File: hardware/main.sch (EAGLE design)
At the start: 10 parts, among them U1 TXB0101_DBV_6

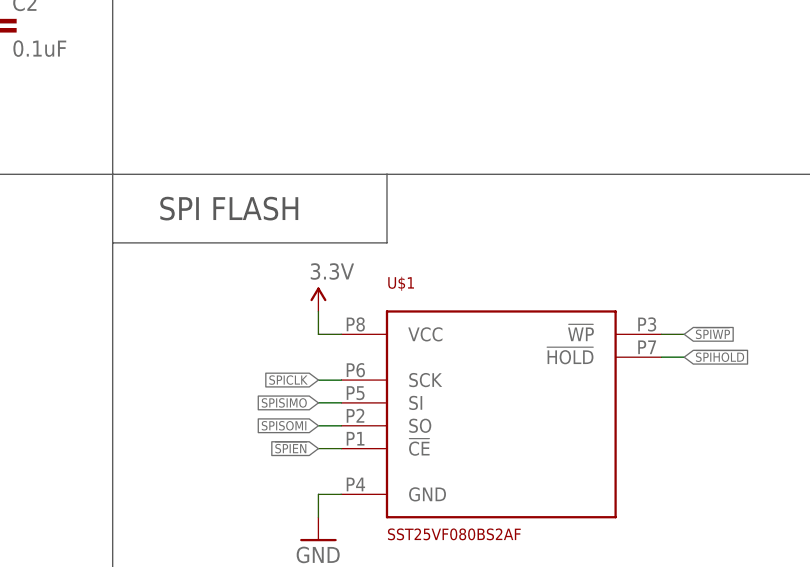
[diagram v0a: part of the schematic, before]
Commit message: Updated small labels. Cleaned up silkscreen layer.
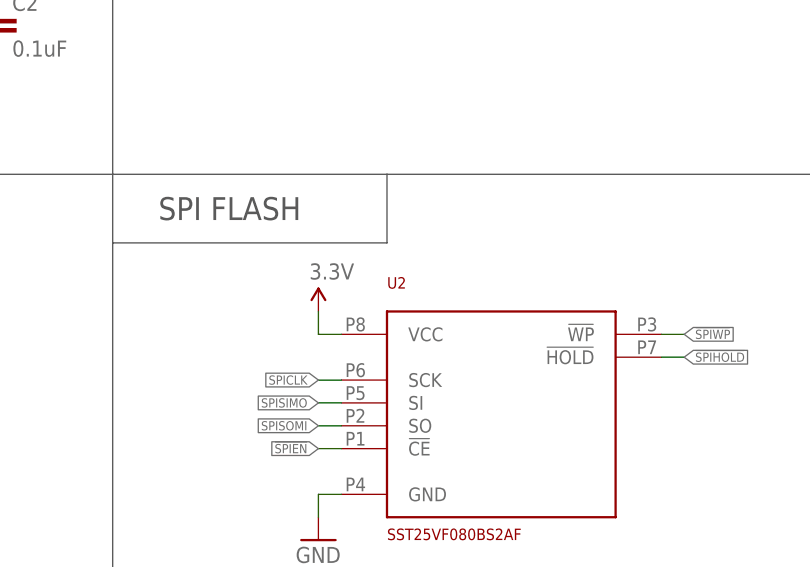
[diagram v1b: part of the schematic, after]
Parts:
- renumbered U$1 to U2
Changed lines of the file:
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@@
 <part name="R2" library="SparkFun-Resistors" deviceset="RESISTOR" device="0805-RES" value="10k"/>
 <part name="C2" library="SparkFun-Capacitors" deviceset="1.0UF-25V-+80/-20(0805)" device="" value="0.1uF"/>
-<part name="U$1" library="ControllerCard" deviceset="SST25VF080B" device="S2AF"/>
+<part name="U2" library="ControllerCard" deviceset="SST25VF080B" device="S2AF"/>
 <part name="SUPPLY6" library="SparkFun-Aesthetics" deviceset="3.3V" device=""/>
 <part name="GND6" library="SparkFun-Aesthetics" deviceset="GND" device=""/>
@@
 <instance part="R2" gate="G$1" x="104.14" y="71.12" rot="R90"/>
 <instance part="C2" gate="G$1" x="119.38" y="68.58"/>
-<instance part="U$1" gate="G$1" x="175.26" y="25.4"/>
+<instance part="U2" gate="G$1" x="175.26" y="25.4"/>
 <instance part="SUPPLY6" gate="G$1" x="154.94" y="38.1"/>
 <instance part="GND6" gate="1" x="154.94" y="12.7"/>
@@
 </segment>
 <segment>
-<pinref part="U$1" gate="G$1" pin="VCC"/>
+<pinref part="U2" gate="G$1" pin="VCC"/>
 <pinref part="SUPPLY6" gate="G$1" pin="3.3V"/>
 <wire x1="157.48" y1="35.56" x2="154.94" y2="35.56" width="0.1524" layer="91"/>
@@
 </segment>
 <segment>
-<pinref part="U$1" gate="G$1" pin="GND"/>
+<pinref part="U2" gate="G$1" pin="GND"/>
 <pinref part="GND6" gate="1" pin="GND"/>
 <wire x1="157.48" y1="17.78" x2="154.94" y2="17.78" width="0.1524" layer="91"/>
@@
 <net name="SPICLK" class="0">
 <segment>
-<pinref part="U$1" gate="G$1" pin="SCK"/>
+<pinref part="U2" gate="G$1" pin="SCK"/>
 <wire x1="157.48" y1="30.48" x2="154.94" y2="30.48" width="0.1524" layer="91"/>
 <label x="154.94" y="30.48" size="1.016" layer="95" rot="R180" xref="yes"/>
@@
 <net name="SPISIMO" class="0">
 <segment>
-<pinref part="U$1" gate="G$1" pin="SI"/>
+<pinref part="U2" gate="G$1" pin="SI"/>
 <wire x1="157.48" y1="27.94" x2="154.94" y2="27.94" width="0.1524" layer="91"/>
 <label x="154.94" y="27.94" size="1.016" layer="95" rot="R180" xref="yes"/>
@@
 <net name="SPISOMI" class="0">
 <segment>
-<pinref part="U$1" gate="G$1" pin="SO"/>
+<pinref part="U2" gate="G$1" pin="SO"/>
 <wire x1="157.48" y1="25.4" x2="154.94" y2="25.4" width="0.1524" layer="91"/>
 <label x="154.94" y="25.4" size="1.016" layer="95" rot="R180" xref="yes"/>
@@
 <net name="!SPIEN!" class="0">
 <segment>
-<pinref part="U$1" gate="G$1" pin="!CE!"/>
+<pinref part="U2" gate="G$1" pin="!CE!"/>
 <wire x1="157.48" y1="22.86" x2="154.94" y2="22.86" width="0.1524" layer="91"/>
 <label x="154.94" y="22.86" size="1.016" layer="95" rot="R180" xref="yes"/>
@@
 <net name="!SPIWP!" class="0">
 <segment>
-<pinref part="U$1" gate="G$1" pin="!WP!"/>
+<pinref part="U2" gate="G$1" pin="!WP!"/>
 <wire x1="193.04" y1="35.56" x2="195.58" y2="35.56" width="0.1524" layer="91"/>
 <label x="195.58" y="35.56" size="1.016" layer="95" xref="yes"/>
@@
 <net name="!SPIHOLD!" class="0">
 <segment>
-<pinref part="U$1" gate="G$1" pin="!HOLD!"/>
+<pinref part="U2" gate="G$1" pin="!HOLD!"/>
 <wire x1="193.04" y1="33.02" x2="195.58" y2="33.02" width="0.1524" layer="91"/>
 <label x="195.58" y="33.02" size="1.016" layer="95" xref="yes"/>

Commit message: Connected pullup resistor on USB
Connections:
- removed net UBSMON: R1.2
- net USBMON: now also R1.2
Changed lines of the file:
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@@
 <label x="30.48" y="76.2" size="1.016" layer="95" rot="R180" xref="yes"/>
 </segment>
-</net>
-<net name="UBSMON" class="0">
 <segment>
 <pinref part="R1" gate="G$1" pin="2"/>

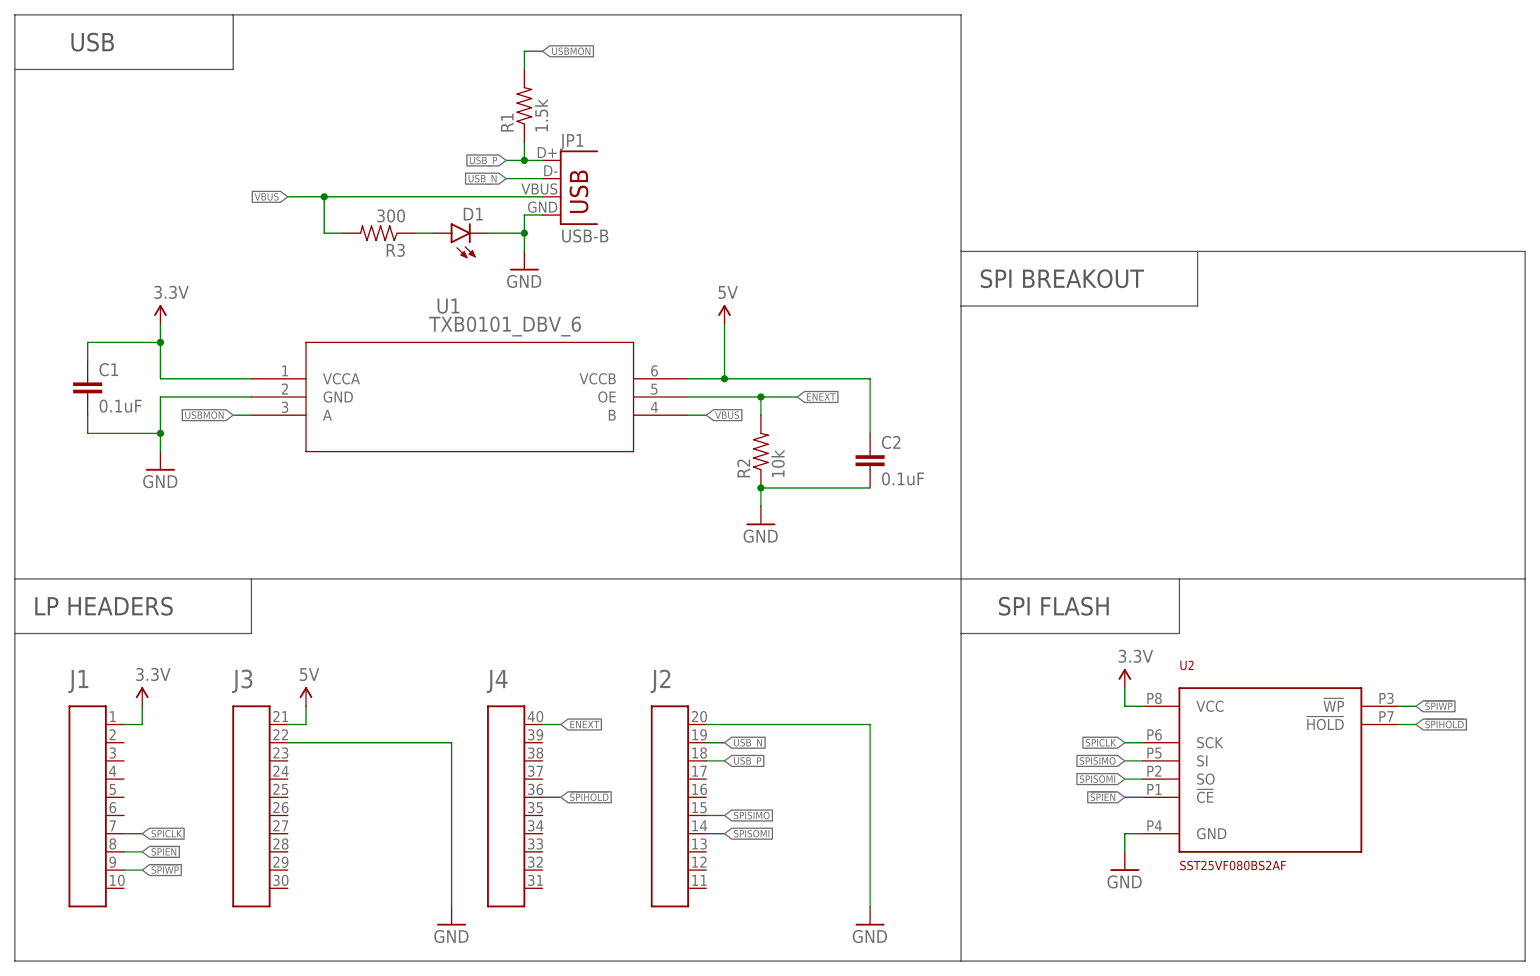
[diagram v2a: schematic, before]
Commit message: Updated routing and USB power
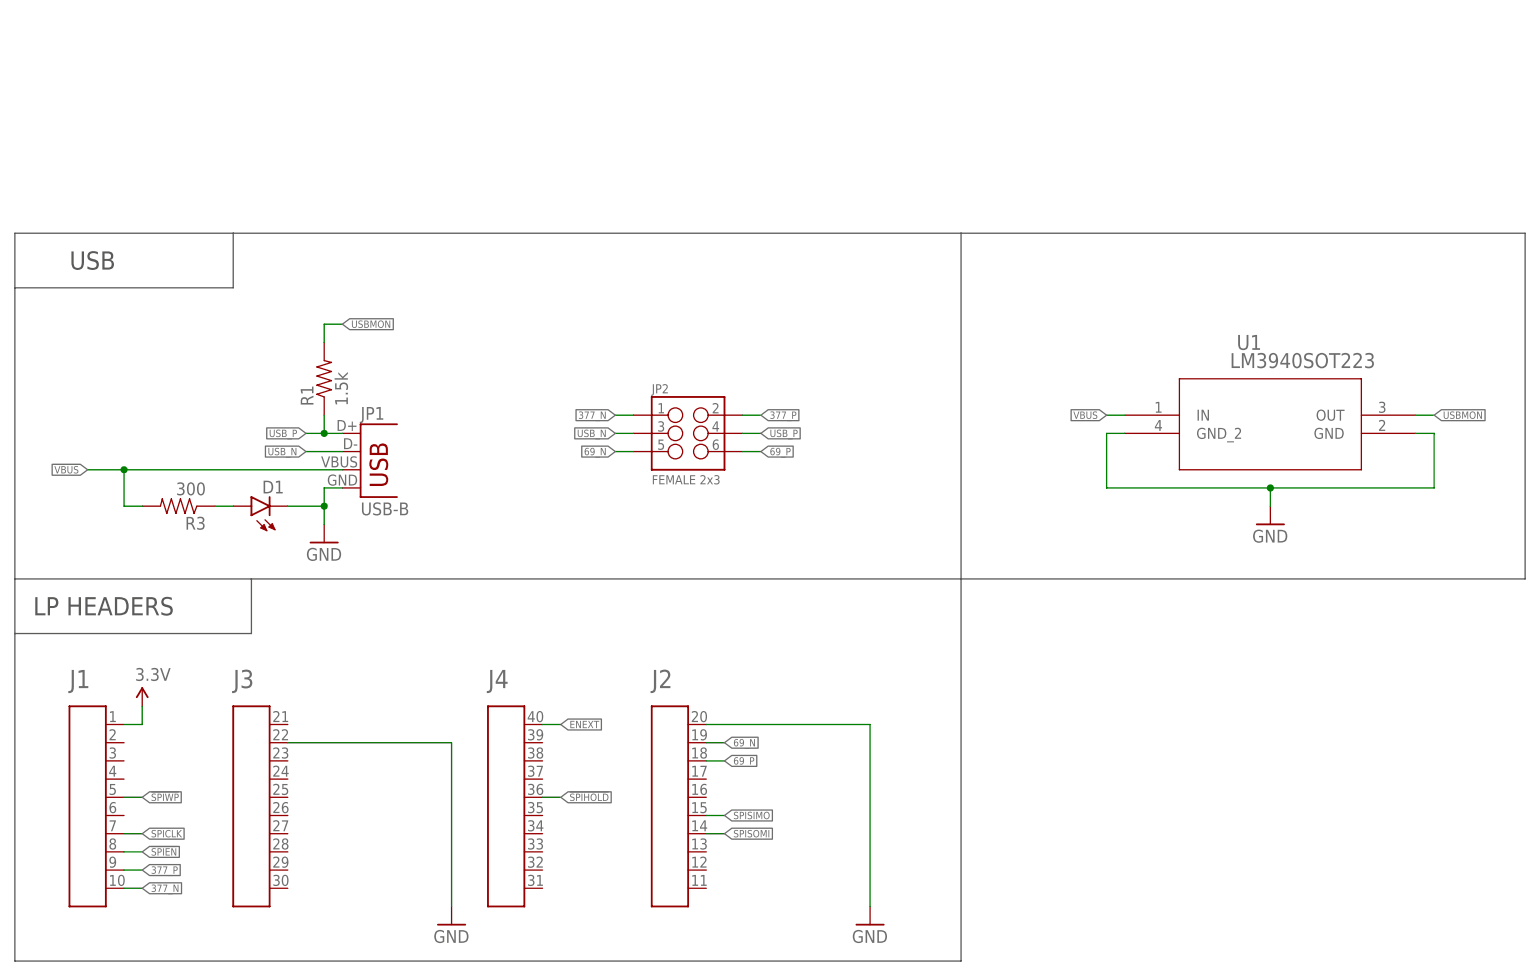
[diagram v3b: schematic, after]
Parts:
- removed C1, C2: 0.1uF, SparkFun-Capacitors:1.0UF-25V-+80/-20(0805)
- removed R2: 10k, SparkFun-Resistors:RESISTOR0805-RES
- removed U2: SST25VF080BS2AF, ControllerCard:SST25VF080BS2AF
- added JP2: FEMALE 2x3, SparkFun-Connectors:M03X2FEMALE
- R1, R3: device SparkFun-Resistors:0.22OHM-1/4W-1%(0805) -> SparkFun-Resistors:1KOHM-1/4W-5%(PTH)
- U1: value TXB0101_DBV_6 -> LM3940SOT223; device ControllerCard:TXB0101_DBV_6 -> ControllerCard:LM3940SOT223
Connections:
- removed net 5V: A1.P$21, C2.1, U1.VCCB
- new net 377_N: A1.P$10, JP2.1
- new net 377_P: A1.P$9, JP2.2
- new net 69_N: A1.P$19, JP2.5
- new net 69_P: A1.P$18, JP2.6
- net !SPIEN!: no longer U2.!CE!
- net !SPIHOLD!: no longer U2.!HOLD!
- net !SPIWP!: now also A1.P$5; no longer A1.P$9, U2.!WP!
- net 3.3V: no longer C1.1, U1.VCCA, U2.VCC
- net ENEXT: no longer R2.2, U1.OE
- net GND: now also U1.GND_2; no longer C1.2, C2.2, R2.1, U2.GND
- net SPICLK: no longer U2.SCK
- net SPISIMO: no longer U2.SI
- net SPISOMI: no longer U2.SO
- net USBMON: now also U1.OUT; no longer U1.A
- net USB_N: now also JP2.3; no longer A1.P$19
- net USB_P: now also JP2.4; no longer A1.P$18
- net VBUS: now also U1.IN; no longer U1.B
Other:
- note removed: "SPI BREAKOUT"
- note removed: "SPI FLASH"
- moved on the sheet: D1, JP1, R1, R3

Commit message: Minor update to component values. Added a BOM
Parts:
- R3: value 300 -> 330
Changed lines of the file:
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@@
 <part name="GND3" library="SparkFun-Aesthetics" deviceset="GND" device=""/>
 <part name="R1" library="SparkFun-Resistors" deviceset="1KOHM-1/4W-5%(PTH)" device="" value="1.5k"/>
-<part name="R3" library="SparkFun-Resistors" deviceset="1KOHM-1/4W-5%(PTH)" device="" value="300"/>
+<part name="R3" library="SparkFun-Resistors" deviceset="1KOHM-1/4W-5%(PTH)" device="" value="330"/>
 <part name="D1" library="SparkFun-LED" deviceset="LED" device="3MM"/>
 <part name="U1" library="ControllerCard" deviceset="LM3940" device="SOT223"/>
